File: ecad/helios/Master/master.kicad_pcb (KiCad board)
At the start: 2 copper layers, 100 x 100 mm, 656 parts, among them J1 MCV 1,5/ 3-G-3,5, J10 MiniFit JR 5556 08A2, J11 MCV 1,5/ 2-G-3,5, J12 MiniFit JR 5556 08A2, J13 M20-8760342, J2 MCV 1,5/ 2-G-3,5, J3 MCV 1,5/ 2-G-3,5, J4 MCV 1,5/ 2-G-3,5, J5 MCV 1,5/ 2-G-3,5, J6 MiniFit JR 5556 08A2, J7 MCV 1,5/ 2-G-3,5, J8 MiniFit JR 5556 08A2, J9 MCV 1,5/ 2-G-3,5, Q1 IRF9Z34NPbF, Q2 BSS84P, Q3 IRF9Z34NPbF, Q4 BSS84P, Q5 IRF9Z34NPbF, Q6 BSS84P, Q7 IRF9Z34NPbF, Q8 BSS84P, SW1 1825910-6, U1 NCP1117-5.0_SOT223, U10 ISO7320FC, U11 UA9638, U12 LM2842Y, U13 LP3985IM5-5.0/NOPB, U14 STEF01FTR, U15 ISO7320FC, U16 UA9638, U17 LM2842Y, U18 LP3985IM5-5.0/NOPB, U19 STEF01FTR, U2 MCP2561-E/SN, U20 ISO7320FC, U21 UA9638, U22 LM2842Y, U23 LP3985IM5-5.0/NOPB, U3 ATMEGA16M1-AU, U4 STEF01FTR, U5 ISO7320FC, U6 UA9638, U7 LM2842Y, U8 LP3985IM5-5.0/NOPB, U9 STEF01FTR, Y1 16MHz

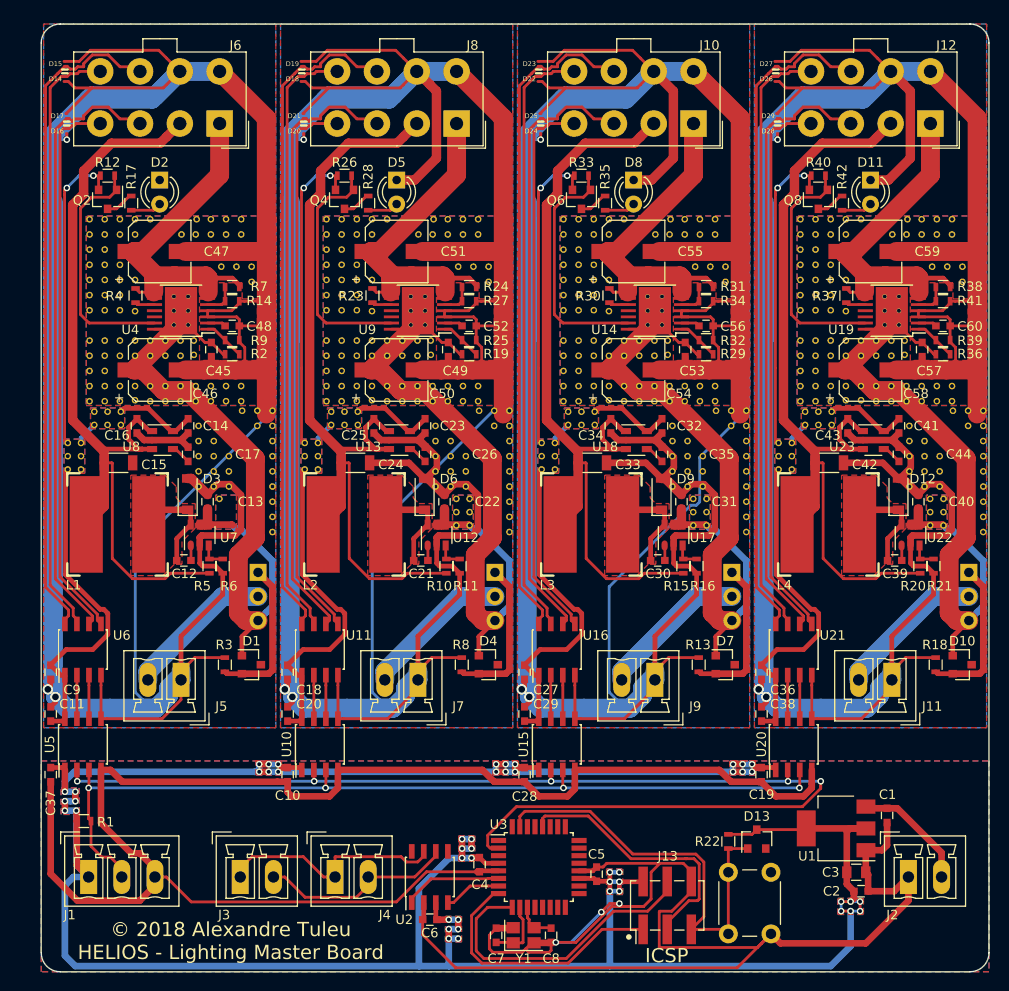
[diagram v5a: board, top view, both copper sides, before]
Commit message: Improves master layout
 * Adds better silkscreen
 * Makes all power connector follow old tracking system +- convention
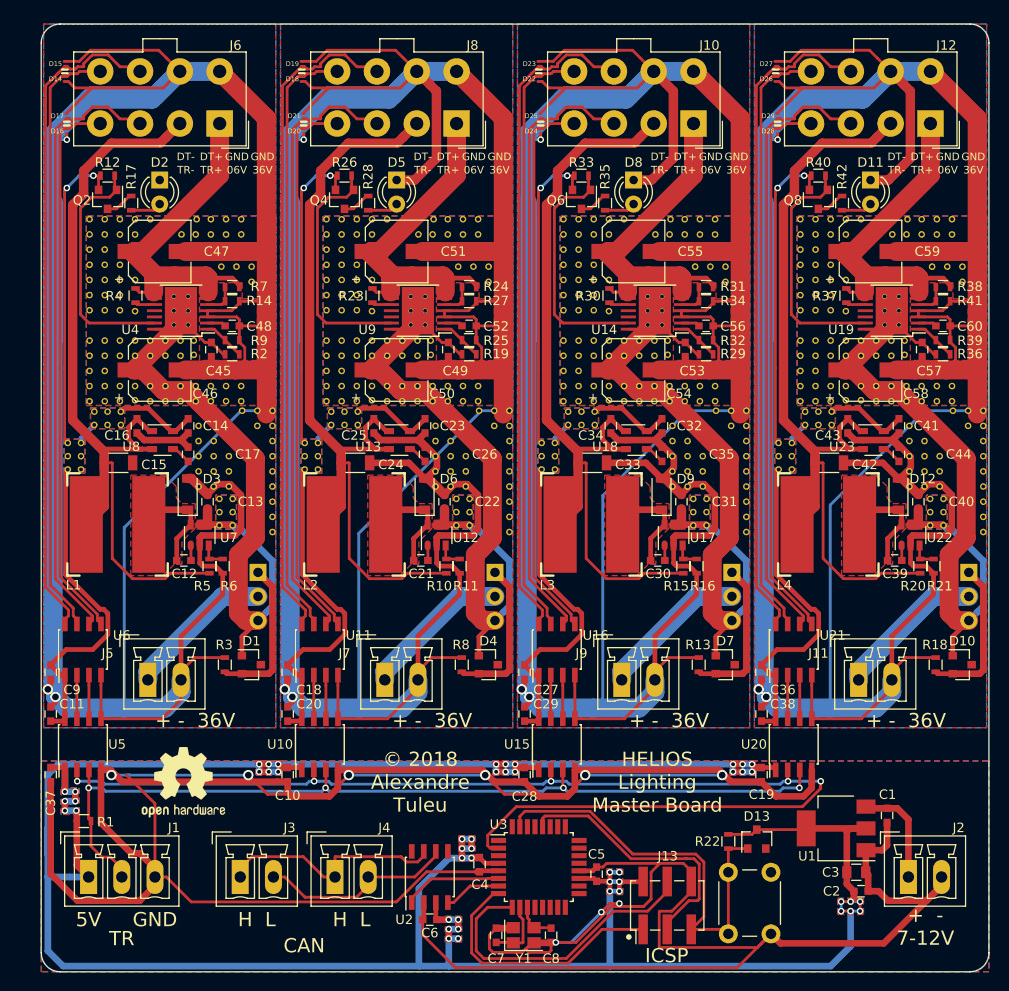
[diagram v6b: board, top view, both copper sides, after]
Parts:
- added REF**: VIA_0.7mm, VIA_0.7mm, F.Cu at (120.2, 102.9)
- added REF**: VIA_0.7mm, VIA_0.7mm, F.Cu at (118.8, 102.9)
- added REF**: VIA_0.7mm, VIA_0.7mm, F.Cu at (120.2, 101.5)
- added REF**: VIA_0.7mm, VIA_0.7mm, F.Cu at (118.8, 101.5)
- added REF**: VIA_0.7mm, VIA_0.7mm, F.Cu at (120.2, 100.1)
- added REF***: OSHW-Logo2_9.8x8mm_SilkScreen, Symbols:OSHW-Logo2_9.8x8mm_SilkScreen, F.Cu at (115.0, 130.0)
- moved J11 3.50 mm to (186.2, 119.2), turned to 0 degrees
- moved J5 3.50 mm to (111.2, 119.2), turned to 0 degrees
- moved J7 3.50 mm to (136.2, 119.2), turned to 0 degrees
- moved J9 3.50 mm to (161.2, 119.2), turned to 0 degrees
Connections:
- J11 pad 1: /Output_1/GNDSUPPLY -> /Output_1/VSUPPLY
- J11 pad 2: /Output_1/VSUPPLY -> /Output_1/GNDSUPPLY
- J2 pad 1: GND -> +12V
- J2 pad 2: +12V -> GND
- J5 pad 1: /Output_2/GNDSUPPLY -> /Output_2/VSUPPLY
- J5 pad 2: /Output_2/VSUPPLY -> /Output_2/GNDSUPPLY
- J7 pad 1: /Output_3/GNDSUPPLY -> /Output_3/VSUPPLY
- J7 pad 2: /Output_3/VSUPPLY -> /Output_3/GNDSUPPLY
- J9 pad 1: /Output_4/GNDSUPPLY -> /Output_4/VSUPPLY
- J9 pad 2: /Output_4/VSUPPLY -> /Output_4/GNDSUPPLY
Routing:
- net GND: track 318.0 -> 404.6 mm, vias 3 -> 9
- net /Output_1/GNDSUPPLY: track 324.7 -> 365.8 mm
- net +5V: track 299.3 -> 313.0 mm
- net /Output_3/GNDSUPPLY: track 367.1 -> 362.9 mm
- net /Output_2/GNDSUPPLY: track 339.5 -> 336.4 mm
- net +12V: track 12.6 -> 11.1 mm
- net /Output_1/TRIGGER: track 94.0 -> 94.9 mm
- net /DATA: track 123.6 -> 124.3 mm
- net /Output_4/GNDSUPPLY: track 366.5 -> 365.8 mm
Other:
- board text added: "+ - 36V"
- board text added: "+ - 7-12V"
- board text added: "06V"
- board text added: "36V"
- board text added: "5V"
- board text added: "CAN"
- board text added: "DT+"
- board text added: "DT-"
- board text added: "GND"
- board text added: "H L"
- board text added: "HELIOS Lighting Master Board"
- board text added: "TR"
- board text added: "TR+"
- board text added: "TR-"
- board text added: "© 2018 Alexandre Tuleu"
- board text removed: "© 2018 Alexandre Tuleu HELIOS - Lighting Master Board"

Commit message: Corrects Master board ICSP pining
Wrong datasheet. This is the correct way to connect a an ICSP to an
ATmega16M1, on the Alternate ICSP, not the primary one, and not on PB3
PB4 PB5 as told in the datasheet.
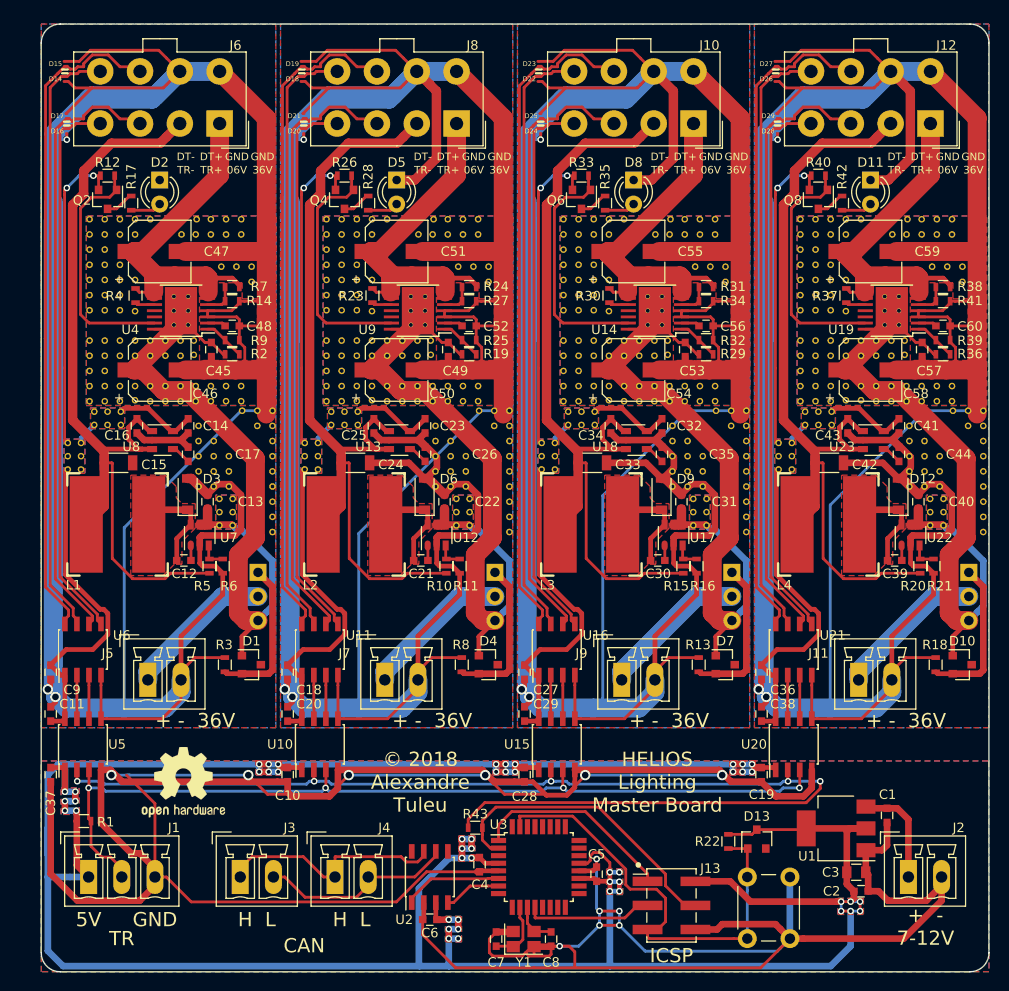
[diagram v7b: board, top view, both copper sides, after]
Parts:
- added R43: 1K, Resistors_SMD:R_0603, F.Cu at (145.8, 134.8)
- moved SW1 2.06 mm to (179.0, 140.0)
- moved J13 0.45 mm to (166.5, 143.0), turned to 0 degrees
- moved C7 0.40 mm to (148.0, 146.6)
- moved C8 0.40 mm to (153.8, 146.6)
- moved Y1 0.40 mm to (150.9, 146.6)
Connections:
- U3 pad 1: (no net) -> /ICSP_MISO
- U3 pad 12: (no net) -> /ICSP_SCK
- U3 pad 2: /DATA -> /ICSP_MOSI
- U3 pad 21: (no net) -> +5V
- U3 pad 28: /ICSP_SCK -> (no net)
- U3 pad 8: /ICSP_MISO -> (no net)
- U3 pad 9: /ICSP_MOSI -> (no net)
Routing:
- net +5V: track 313.0 -> 332.2 mm
- net /ICSP_SCK: track 28.6 -> 13.5 mm
- net /ICSP_MISO: track 27.8 -> 21.5 mm
- net /~ICSP_RESET: track 45.8 -> 50.0 mm
- net GND: track 404.6 -> 405.9 mm, vias 9 -> 12

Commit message: Updates silkscreens
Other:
- board text added: "HELIOS Lighting Master Board rev B"
- board text removed: "HELIOS Lighting Master Board"
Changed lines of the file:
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@@
   (general
     (links 940)
-    (no_connects 1)
+    (no_connects 0)
     (area 99.924999 49.924999 200.075001 150.075001)
     (thickness 1.6)
@@
     (tags "capacitor 0603")
     (attr smd)
-    (fp_text reference C1 (at -2.2 -0.05 360) (layer F.SilkS)
+    (fp_text reference C1 (at 0 -2 360) (layer F.SilkS)
       (effects (font (size 1 1) (thickness 0.15)))
     )
@@
     (effects (font (size 1.5 1.5) (thickness 0.3)))
   )
-  (gr_text "HELIOS\nLighting \nMaster Board" (at 165 130) (layer F.SilkS)
+  (gr_text "HELIOS\nLighting \nMaster Board\nrev B" (at 165 130) (layer F.SilkS)
     (effects (font (size 1.5 1.5) (thickness 0.3)))
   )
